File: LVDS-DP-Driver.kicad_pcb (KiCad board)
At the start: 2 copper layers, 50 x 50 mm, 122 parts, among them J1 47272-0001, J2 Conn_02x15_Odd_Even, J3 Conn_01x06_Male, J4 Conn_01x03_Male, J5 Conn_01x04_Male, J6 Conn_01x03_Male, Q1 Si4816BDY, Q10 2N7002, Q2 Si4816BDY, Q3 Si4816BDY, Q4 MMBT3904, Q5 MMBT3904, Q6 2N7002, Q7 AO3401A, Q8 2N7002, Q9 2N7002, SW1 SW_DIP_x04, U1 CS5211, U2 LTC3853, U3 AT24C64

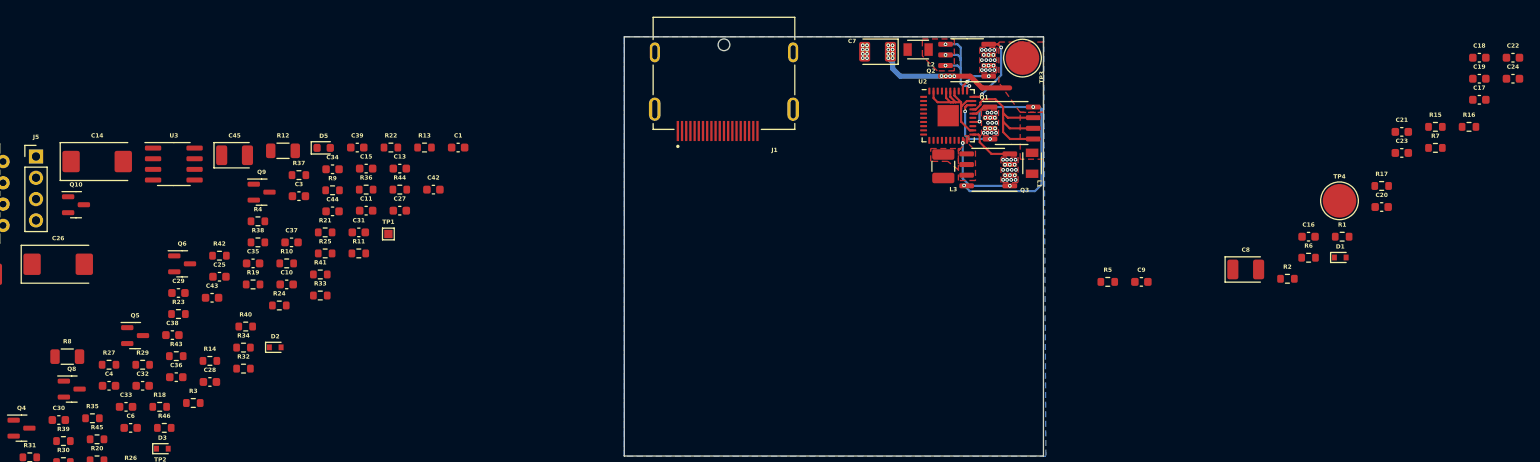
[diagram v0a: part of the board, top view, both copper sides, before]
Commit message: Buck layout 60%
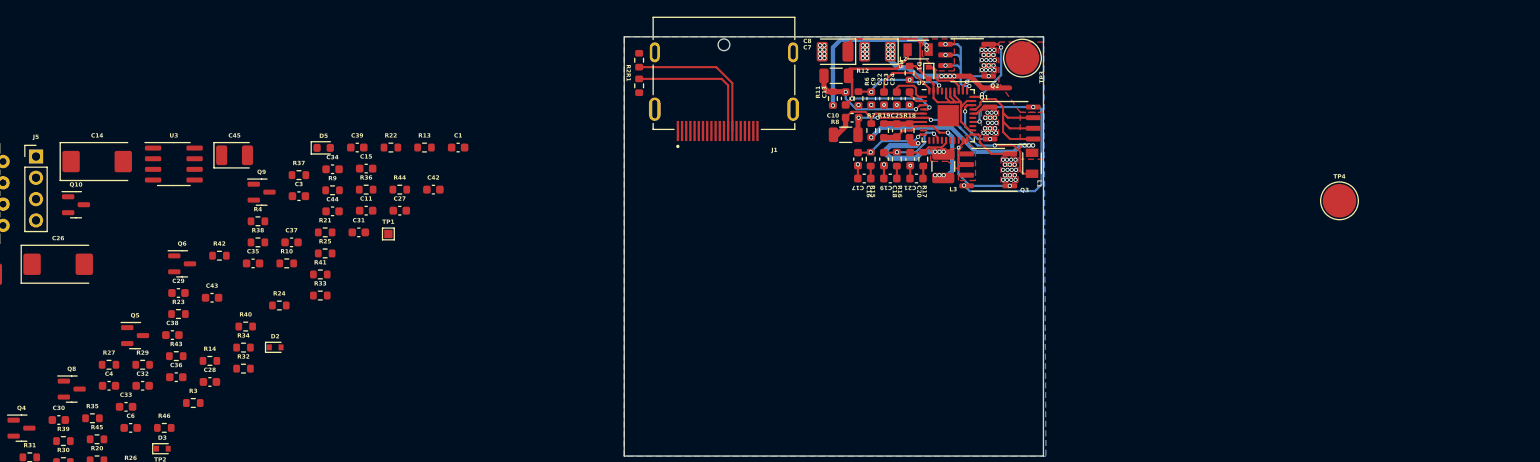
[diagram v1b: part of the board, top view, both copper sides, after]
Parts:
- moved R8 96.5 mm to (151.1, 27.4)
- moved R18 95.3 mm to (158.8, 26.9), turned to 90 degrees
- moved R1 85.8 mm to (126.5, 21.6), turned to -90 degrees
- moved C25 82.7 mm to (157.2, 26.9), turned to -90 degrees
- moved R2 81.6 mm to (126.5, 18.5), turned to 90 degrees
- moved R19 77.5 mm to (155.7, 26.9), turned to -90 degrees
- moved C22 75.2 mm to (155.7, 23.1), turned to -90 degrees
- moved C17 74.0 mm to (153.3, 32.6), turned to 180 degrees
- moved C18 72.0 mm to (155.7, 30.3), turned to -90 degrees
- moved C24 72.0 mm to (158.8, 23.1), turned to 90 degrees
- moved C19 71.3 mm to (156.4, 32.6), turned to 180 degrees
- moved C10 70.3 mm to (151.9, 25.4)
- moved R16 68.4 mm to (157.2, 30.3), turned to -90 degrees
- moved R15 67.5 mm to (154.1, 30.3), turned to -90 degrees
- moved R7 67.3 mm to (154.2, 26.9), turned to 90 degrees
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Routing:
- net +3V3: track 0.00 -> 27.0 mm, vias 0 -> 4
- net +5V: track 0.00 -> 23.8 mm, vias 0 -> 2
- net Net-(Q1-C): track 19.8 -> 41.1 mm, vias 0 -> 4
- net Net-(Q2-C): track 12.3 -> 31.6 mm, vias 4 -> 7
- net Net-(D1-A): track 15.6 -> 33.5 mm
- net Net-(J1-Pad14): track 0.00 -> 17.6 mm
- net Net-(J1-Pad13): track 0.00 -> 16.4 mm
- net +1V8: track 0.00 -> 15.5 mm, vias 0 -> 4
- net /SEN1+: track 0.00 -> 15.0 mm, vias 0 -> 2
- net /SEN2+: track 0.00 -> 13.7 mm
- net /SW3: track 0.00 -> 13.6 mm, vias 0 -> 4
- net Net-(U2-FREQ): track 0.00 -> 11.4 mm, vias 0 -> 3
- net Net-(U2-ITH1): track 0.00 -> 8.65 mm, vias 0 -> 2
- net Net-(U2-ITH2): track 0.00 -> 8.56 mm, vias 0 -> 2
- net Net-(U2-SS1): track 0.00 -> 8.15 mm
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
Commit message: Buck Components
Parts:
- moved C12 126.0 mm to (172.2, 39.4), turned to -90 degrees
- moved C26 99.4 mm to (156.5, 37.3), turned to 180 degrees
- moved D3 97.6 mm to (156.7, 20.8)
- moved C28 93.4 mm to (166.1, 35.3)
- moved D2 91.0 mm to (168.9, 22.6)
- moved R20 88.3 mm to (143.1, 31.8), turned to -90 degrees
- moved C29 86.2 mm to (153.9, 20.8), turned to 180 degrees
- moved R14 77.9 mm to (150.1, 32.6)
- moved R10 63.4 mm to (147.1, 32.6)
- moved R9 58.0 mm to (147.8, 30.3), turned to -90 degrees
- moved R21 56.2 mm to (144.7, 31.8), turned to 90 degrees
- moved C15 55.4 mm to (149.4, 30.3), turned to -90 degrees
- moved C11 52.7 mm to (146.3, 30.3), turned to -90 degrees
- moved R13 50.0 mm to (150.9, 30.3), turned to -90 degrees
- moved C14 49.7 mm to (111.5, 28.2), turned to 90 degrees
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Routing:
- net Net-(D3-K): track 0.00 -> 42.0 mm, vias 0 -> 2
- net Net-(D2-K): track 0.00 -> 40.3 mm, vias 0 -> 3
- net Net-(D1-K): track 5.59 -> 34.5 mm, vias 0 -> 4
- net /FB2: track 0.00 -> 28.0 mm, vias 0 -> 2
- net GND: track 4.63 -> 32.1 mm, vias 76 -> 169
- net /FB3: track 0.00 -> 27.3 mm, vias 0 -> 2
- net Net-(D1-A): track 33.5 -> 59.2 mm, vias 0 -> 5
- net +1V8: track 15.5 -> 39.3 mm, vias 4 -> 7
- net /FB1: track 0.00 -> 15.4 mm, vias 0 -> 2
- net /SW3: track 13.6 -> 28.9 mm
- net +3V3: track 27.0 -> 39.8 mm, vias 4 -> 5
- net +5V: track 23.8 -> 33.3 mm, vias 2 -> 4
- net Net-(Q2-C): track 31.6 -> 39.4 mm, vias 7 -> 8
- net Net-(Q1-C): track 41.1 -> 48.0 mm
- net +12V: track 49.8 -> 48.5 mm, vias 15 -> 13
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- added copper zone on F.Cu, net +1V8
- added copper zone on F.Cu, net +3V3
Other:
- board text added: "-L-"
- board text added: "-M-"
- board text added: "-R-"

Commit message: LVDS routing and layouting misc
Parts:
- added G0: R_0603_1608Metric, Resistor_SMD:R_0603_1608Metric, F.Cu at (159.0, 44.7)
- added G1: R_0603_1608Metric, Resistor_SMD:R_0603_1608Metric, F.Cu at (161.5, 44.7)
- added G2: R_0603_1608Metric, Resistor_SMD:R_0603_1608Metric, F.Cu at (164.1, 44.7)
- added G3: R_0603_1608Metric, Resistor_SMD:R_0603_1608Metric, F.Cu at (166.6, 44.7)
- J3: footprint Connector_PinHeader_2.54mm:PinHeader_1x06_P2.54mm_Vertical -> Connector_PinHeader_2.00mm:PinHeader_1x06_P2.00mm_Vertical
- moved J3 132.4 mm to (167.8, 60.7), turned to -90 degrees
- moved J2 124.1 mm to (154.2, 55.1), turned to -90 degrees
- moved J5 120.8 mm to (172.7, 55.1), turned to 180 degrees
- moved J6 117.9 mm to (161.6, 53.8), turned to 90 degrees
- moved SW1 117.4 mm to (159.0, 48.5), turned to 90 degrees
- moved J4 115.6 mm to (154.7, 46.5)
- moved R28 111.1 mm to (167.4, 50.5), turned to 180 degrees
- moved R31 105.6 mm to (158.2, 50.5)
- moved R30 104.7 mm to (161.3, 50.5)
- moved U1 102.4 mm to (135.2, 40.4)
- moved Q10 100.7 mm to (157.7, 56.9)
- moved R29 97.2 mm to (164.3, 50.5)
- moved C5 92.5 mm to (138.9, 32.3), turned to -90 degrees
- moved D4 91.0 mm to (125.6, 28.7), turned to 90 degrees
- moved C45 88.5 mm to (162.3, 57.4), turned to 180 degrees
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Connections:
- net Net-(U1A-AUXN) renamed AUXN
- net Net-(U1A-AUXP) renamed AUXP
- net Net-(U1A-DP0N) renamed DP0N
- net Net-(U1A-DP0P) renamed DP0P
- net Net-(U1A-DP1N) renamed DP1N
- net Net-(U1A-DP1P) renamed DP1P
- J4 pad 3: +3.3V -> +3V3
- Q6 pad 1: +3.3V -> +3V3
- R22 pad 1: +3.3V -> +3V3
- R27 pad 1: +3.3V -> +3V3
- R28 pad 1: +3.3V -> +3V3
- R29 pad 1: +3.3V -> +3V3
- R30 pad 1: +3.3V -> +3V3
- R31 pad 1: +3.3V -> +3V3
- R39 pad 1: +3.3V -> +3V3
- R40 pad 1: +3.3V -> +3V3
- R41 pad 1: +3.3V -> +3V3
- R42 pad 1: +3.3V -> +3V3
- R43 pad 1: +3.3V -> +3V3
- R44 pad 1: +3.3V -> +3V3
- R45 pad 2: +3.3V -> +3V3
- R46 pad 2: +3.3V -> +3V3
- U3 pad 8: +3.3V -> +3V3
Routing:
- net +5V: track 33.3 -> 165.8 mm, vias 4 -> 16
- net +3V3: track 39.8 -> 153.3 mm, vias 5 -> 14
- net /BLDN: track 0.00 -> 90.3 mm, vias 0 -> 7
- net +1V8: track 39.3 -> 117.6 mm, vias 7 -> 10
- net /PWRDN: track 0.00 -> 61.7 mm, vias 0 -> 3
- net /BKUP_BTN: track 0.00 -> 57.6 mm, vias 0 -> 3
- net GND: track 32.1 -> 82.8 mm, vias 169 -> 240
- net /EN_BKLT: track 0.00 -> 40.6 mm, vias 0 -> 2
- net +12V: track 48.5 -> 83.9 mm, vias 13 -> 14
- net /GPIO3: track 0.00 -> 34.8 mm, vias 0 -> 2
- net /GPIO2: track 0.00 -> 32.5 mm, vias 0 -> 2
- net /GPIO1: track 0.00 -> 29.9 mm, vias 0 -> 2
- net /GPIO0: track 0.00 -> 28.1 mm, vias 0 -> 2
- net /P_BKLT_EN: track 0.00 -> 25.4 mm
- net /E2_SDA: track 0.00 -> 23.3 mm, vias 0 -> 2
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- added copper zone on F.Cu, net /LCD_BKLT_VCC
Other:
- board size 50 x 50 mm -> 50 x 46.7 mm
- board text added: "U"

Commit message: Finished routing
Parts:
- moved Q7 97.5 mm to (145.3, 50.3), turned to 180 degrees
- moved Q8 85.3 mm to (144.1, 60.5)
- moved C38 82.4 mm to (146.6, 18.8), turned to 90 degrees
- moved R35 80.1 mm to (141.4, 60.3), turned to 90 degrees
- moved C30 77.4 mm to (134.6, 60.2), turned to 90 degrees
- moved C39 73.6 mm to (165.9, 38.4)
- moved C40 73.4 mm to (137.9, 60.5), turned to 180 degrees
- moved Q9 71.6 mm to (148.1, 60.5), turned to 180 degrees
- moved C33 64.8 mm to (130.0, 60.2), turned to 90 degrees
- moved C32 64.4 mm to (131.6, 60.2), turned to 90 degrees
- moved R34 63.3 mm to (142.5, 50.0), turned to 90 degrees
- moved C37 63.2 mm to (147.1, 27.9)
- moved R33 59.7 mm to (148.1, 50.3), turned to -90 degrees
- moved C36 54.3 mm to (125.5, 60.2), turned to -90 degrees
- moved R36 50.5 mm to (142.7, 47.0), turned to 90 degrees
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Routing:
- net +3V3: track 153.3 -> 233.5 mm, vias 14 -> 20
- net +1V8: track 117.6 -> 177.1 mm, vias 10 -> 17
- net /EN_VCC: track 0.00 -> 56.3 mm, vias 0 -> 6
- net HT: track 7.96 -> 53.4 mm, vias 0 -> 13
- net /PWM0: track 4.55 -> 46.5 mm, vias 2 -> 6
- net Net-(Q8-D): track 0.00 -> 34.3 mm, vias 0 -> 2
- net Net-(Q9-D): track 0.00 -> 30.5 mm, vias 0 -> 2
- net GND: track 82.8 -> 99.2 mm, vias 240 -> 280
- net Net-(J4-Pin_2): track 0.00 -> 9.52 mm, vias 0 -> 1
- net /B0N: track 12.3 -> 21.4 mm
- net /A3N: track 12.6 -> 21.4 mm
- net /ACLKN: track 13.1 -> 21.2 mm
- net /B1N: track 13.8 -> 21.3 mm
- net /B0P: track 14.9 -> 21.5 mm
- net /B2N: track 14.9 -> 21.2 mm
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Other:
- outline, holes or cut-outs redrawn

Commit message: Changed License to SHL
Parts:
- added REF**: OSHW-Logo_5.7x6mm_SilkScreen, Symbol:OSHW-Logo_5.7x6mm_SilkScreen, F.Cu at (131.1, 48.5)
- added REF**: Symbol_Highvoltage_Type1_CopperTop_Small, Symbol:Symbol_Highvoltage_Type1_CopperTop_Small, B.Cu at (130.6, 19.6)
- added REF**: OSHW-Logo2_7.3x6mm_Copper, Symbol:OSHW-Logo2_7.3x6mm_Copper, B.Cu at (139.2, 19.1)

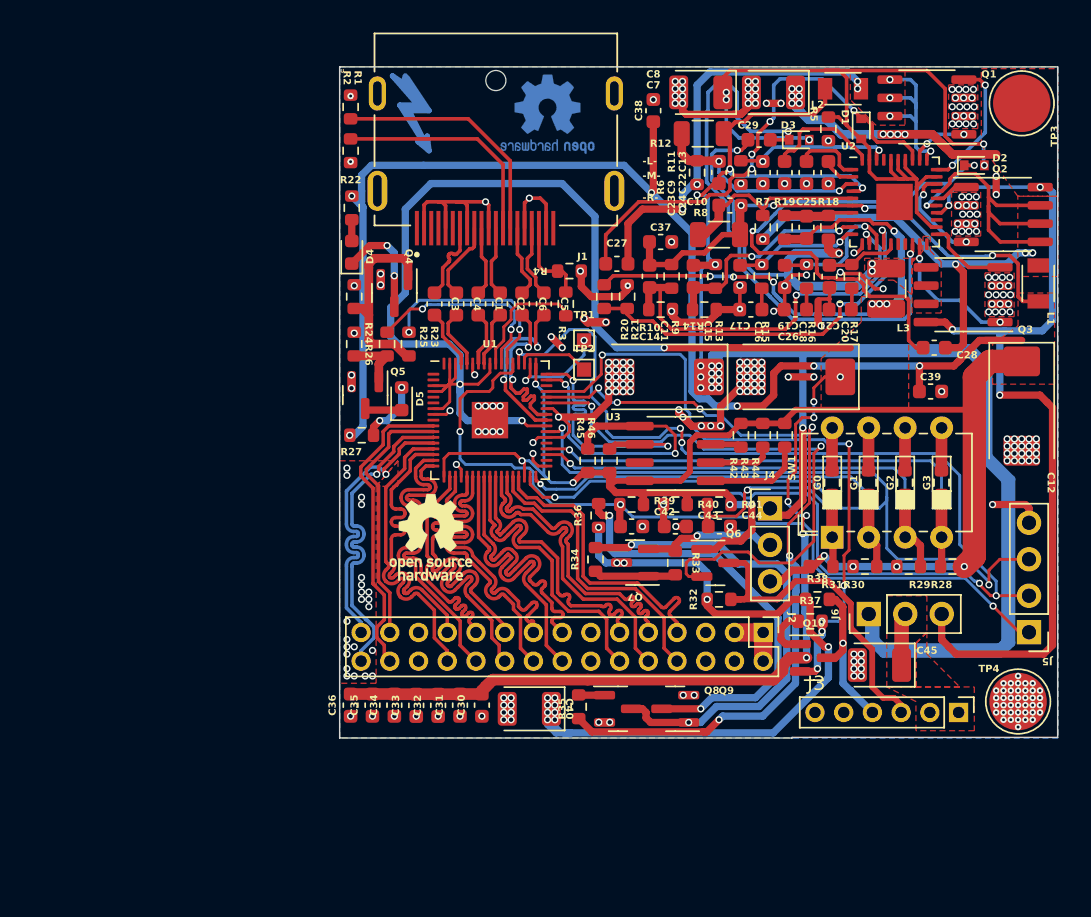
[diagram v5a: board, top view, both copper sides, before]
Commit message: assigned footprints
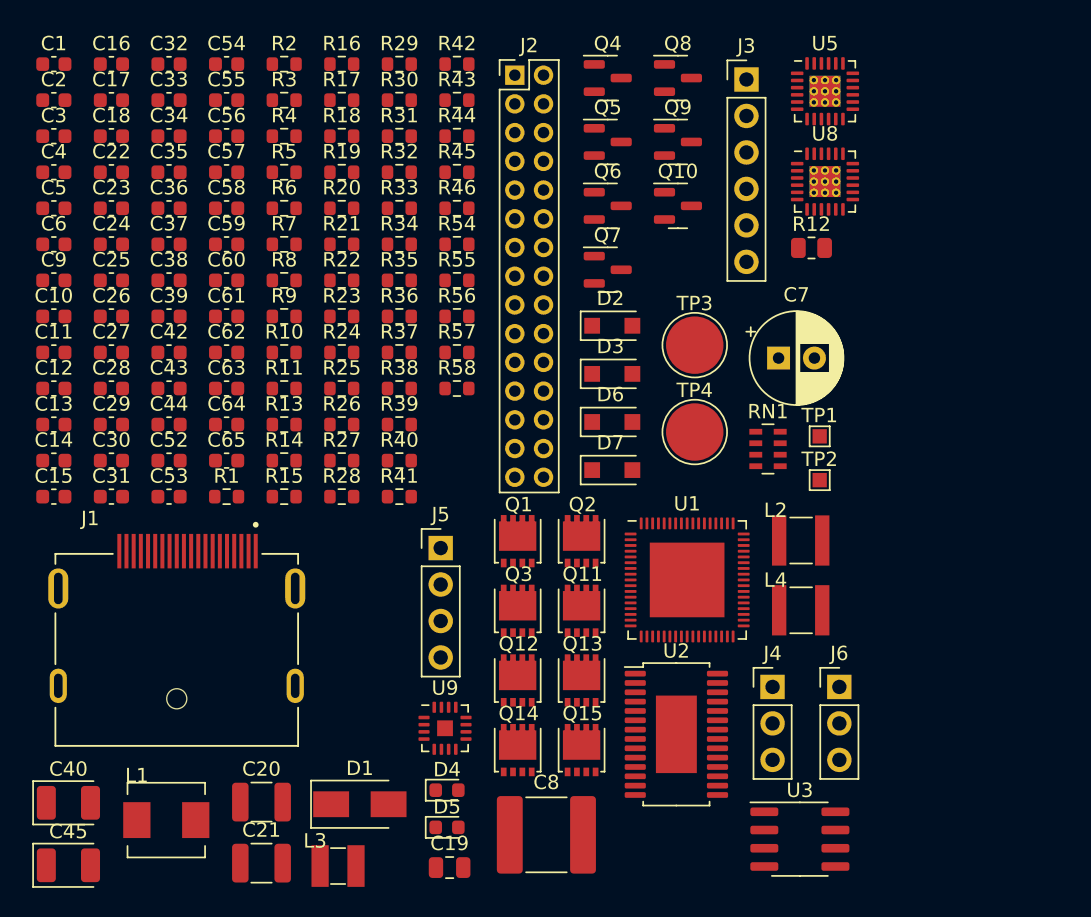
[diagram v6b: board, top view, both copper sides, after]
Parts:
- removed G0, G1, G2, G3: R_0603_1608Metric, Resistor_SMD:R_0603_1608Metric
- removed REF**: OSHW-Logo_5.7x6mm_SilkScreen, Symbol:OSHW-Logo_5.7x6mm_SilkScreen
- removed REF**: Symbol_Highvoltage_Type1_CopperTop_Small, Symbol:Symbol_Highvoltage_Type1_CopperTop_Small
- removed REF**: OSHW-Logo2_7.3x6mm_Copper, Symbol:OSHW-Logo2_7.3x6mm_Copper
- removed SW1: SW_DIP_x04, Button_Switch_THT:SW_DIP_SPSTx04_Slide_6.7x11.72mm_W7.62mm_P2.54mm_LowProfile
- added C52: 4.7nF, Capacitor_SMD:C_0603_1608Metric, F.Cu at (112.8, 43.2)
- added C53: 10uF, Capacitor_SMD:C_0603_1608Metric, F.Cu at (112.8, 45.7)
- added C54: 10uF, Capacitor_SMD:C_0603_1608Metric, F.Cu at (116.8, 15.6)
- added C55: 3.3nF, Capacitor_SMD:C_0603_1608Metric, F.Cu at (116.8, 18.1)
- added C56: 100nF, Capacitor_SMD:C_0603_1608Metric, F.Cu at (116.8, 20.6)
- added C57: 33pF, Capacitor_SMD:C_0603_1608Metric, F.Cu at (116.8, 23.1)
- added C58: 2.2uF, Capacitor_SMD:C_0603_1608Metric, F.Cu at (116.8, 25.6)
- added C59: 39nF, Capacitor_SMD:C_0603_1608Metric, F.Cu at (116.8, 28.1)
- added C60: 220nF, Capacitor_SMD:C_0603_1608Metric, F.Cu at (116.8, 30.6)
- added C61: 100nF, Capacitor_SMD:C_0603_1608Metric, F.Cu at (116.8, 33.1)
- added C62: 220pF, Capacitor_SMD:C_0603_1608Metric, F.Cu at (116.8, 35.6)
- added C63: 10uF, Capacitor_SMD:C_0603_1608Metric, F.Cu at (116.8, 38.1)
- added C64: 100nF, Capacitor_SMD:C_0603_1608Metric, F.Cu at (116.8, 40.7)
- added C65: 22uF, Capacitor_SMD:C_0603_1608Metric, F.Cu at (116.8, 43.2)
- added D6: DSK12, Diode_SMD:D_SOD-123F, F.Cu at (143.7, 40.5)
- added D7: DSK12, Diode_SMD:D_SOD-123F, F.Cu at (143.7, 43.8)
- added L4: CKST353220-2.2uH/M, Footprints:CKST353220, F.Cu at (155.1, 52.0)
- added Q11: AGM612AP, Footprints:PDFN8_3x3, F.Cu at (141.6, 53.6)
- added Q12: AGM308AP, Footprints:PDFN8_3x3, F.Cu at (137.2, 58.5)
- added Q13: AGM308AP, Footprints:PDFN8_3x3, F.Cu at (141.6, 58.5)
- added Q14: AGM308AP, Footprints:PDFN8_3x3, F.Cu at (137.2, 63.3)
- added Q15: AGM308AP, Footprints:PDFN8_3x3, F.Cu at (141.6, 63.3)
- added R54: 10R, Resistor_SMD:R_0603_1608Metric, F.Cu at (132.9, 28.1)
- added R55: 2K32, Resistor_SMD:R_0603_1608Metric, F.Cu at (132.9, 30.6)
- added R56: 10K, Resistor_SMD:R_0603_1608Metric, F.Cu at (132.9, 33.1)
- added R57: 187K, Resistor_SMD:R_0603_1608Metric, F.Cu at (132.9, 35.6)
- added R58: 150K, Resistor_SMD:R_0603_1608Metric, F.Cu at (132.9, 38.1)
- added RN1: R_Pack04, Resistor_SMD:R_Array_Concave_4x0603, F.Cu at (154.5, 42.4)
- added U5: LM25141, Package_DFN_QFN:QFN-24-1EP_4x4mm_P0.5mm_EP2.15x2.15mm_ThermalVias, F.Cu at (158.5, 17.4)
- added U8: LM25141, Package_DFN_QFN:QFN-24-1EP_4x4mm_P0.5mm_EP2.15x2.15mm_ThermalVias, F.Cu at (158.5, 23.7)
- added U9: TLV62130, Package_DFN_QFN:VQFN-16-1EP_3x3mm_P0.5mm_EP1.1x1.1mm, F.Cu at (132.1, 61.8)
- C10: value 100nF -> 15nF
- C11: value 10pF -> 100pF
- C12: value 330uF -> 6.8nF; footprint Capacitor_Tantalum_SMD:CP_EIA-7343-31_Kemet-D -> Capacitor_SMD:C_0603_1608Metric
- C13: value 100nF -> 82pF
- C14: value 330uF -> 100nF; footprint Capacitor_Tantalum_SMD:CP_EIA-7343-31_Kemet-D -> Capacitor_SMD:C_0603_1608Metric
- C15: value 10pF -> 47pF
- C16: value 220pF -> 100nF
- C17: value 1.5nF -> 100nF
- C18: value 220pF -> 1uF
- C19: value 1.5nF -> 22uF * 3; footprint Capacitor_SMD:C_0603_1608Metric -> Capacitor_SMD:C_0805_2012Metric
- C20: value 330pF -> 47uF; footprint Capacitor_SMD:C_0603_1608Metric -> Capacitor_SMD:C_1210_3225Metric
- C21: value 1.5nF -> 47uF; footprint Capacitor_SMD:C_0603_1608Metric -> Capacitor_SMD:C_1210_3225Metric
- C22: value 100nF -> 10uF
- C24: value 100nF -> 39nF
- C25: value 68nF -> 220nF
- C26: value 330uF -> 2.2uF; footprint Capacitor_Tantalum_SMD:CP_EIA-7343-31_Kemet-D -> Capacitor_SMD:C_0603_1608Metric
- C28: value 100nF -> 4.7uF
- C29: value 100nF -> 56pF
- C7: value 22uF -> 68uF; footprint Capacitor_Tantalum_SMD:CP_EIA-3528-21_Kemet-B -> Capacitor_THT:CP_Radial_D6.3mm_P2.50mm
- C8: value 4.7uF -> 10uF * 3; footprint Capacitor_Tantalum_SMD:CP_EIA-3528-21_Kemet-B -> Capacitor_SMD:C_2220_5650Metric
- C9: value 1nF -> 100nF
- D1: value D_Schottky -> MBR180S1-7; footprint Diode_SMD:D_SOD-523 -> Diode_SMD:D_SMA
- D2: value D_Schottky -> DSK12; footprint Diode_SMD:D_SOD-523 -> Diode_SMD:D_SOD-123F
- D3: value D_Schottky -> RB160MM-90TR; footprint Diode_SMD:D_SOD-523 -> Diode_SMD:D_SOD-123F
- J3: footprint Connector_PinHeader_2.00mm:PinHeader_1x06_P2.00mm_Vertical -> Connector_PinHeader_2.54mm:PinHeader_1x06_P2.54mm_Vertical
- L1: value 3.3uH -> CYA0650-3.3UH; footprint Inductor_SMD:L_TDK_NLV25_2.5x2.0mm -> Footprints:L_0530
- L2: value 3.3uH -> CKST353220-2.2uH/M; footprint Inductor_SMD:L_TDK_NLV25_2.5x2.0mm -> Footprints:CKST353220
- L3: value 1.5uH -> CKST322512-1uH/M; footprint Inductor_SMD:L_1210_3225Metric -> Footprints:CKST322512
- Q1, Q2, Q3: value Si4816BDY -> AGM612AP; footprint Package_SO:SO-8_3.9x4.9mm_P1.27mm -> Footprints:PDFN8_3x3
- R10: value 20K -> 93K1
- R11: value 4.75K -> 13K
- R12: value 1430 -> 15m; footprint Resistor_SMD:R_1206_3216Metric -> Resistor_SMD:R_0805_2012Metric
- R13: value 105K -> 100R
- R14: value 20K -> 100R
- R15: value 15K -> 10K
- R16: value 18K -> 280K
- R17: value 10K -> 20K
- R18: value 2.43K -> 10R
- R19: value 1.82K -> 12m
- R20: value 25K -> 1K62
- R21: value 20K -> 10m
- R5: value 10K -> 249K
- R6: value 3.16K -> 42K2
- R7: value 4.75K -> 2K
- R8: value 1430 -> 10R; footprint Resistor_SMD:R_1206_3216Metric -> Resistor_SMD:R_0603_1608Metric
- R9: value 63.4K -> 6K19
- U2: value LTC3853 -> LM5176; footprint Package_DFN_QFN:QFN-40-1EP_6x6mm_P0.5mm_EP4.6x4.6mm -> Package_SO:HTSSOP-28-1EP_4.4x9.7mm_P0.65mm_EP2.85x5.4mm
- moved L1 71.8 mm to (110.6, 65.6), turned to 0 degrees
- moved C12 67.4 mm to (104.8, 38.1), turned to 0 degrees
- moved D1 58.6 mm to (126.1, 67.1), turned to 0 degrees
- moved C45 58.2 mm to (105.8, 71.3), turned to 0 degrees
- moved C28 57.4 mm to (108.8, 38.1)
- moved C21 55.8 mm to (119.3, 71.2), turned to 0 degrees
- moved L3 55.7 mm to (123.0, 70.2), turned to 0 degrees
- moved J1 54.4 mm to (113.4, 63.0), turned to 0 degrees
- moved C20 53.9 mm to (119.3, 66.9), turned to 0 degrees
- moved C39 53.3 mm to (112.8, 33.1)
- moved C8 52.8 mm to (139.1, 69.2), turned to 0 degrees
- moved C24 50.2 mm to (108.8, 28.1), turned to 0 degrees
- moved C9 49.9 mm to (104.8, 30.6), turned to 0 degrees
- moved R29 49.8 mm to (128.9, 15.6)
- moved C13 49.5 mm to (104.8, 40.7), turned to 0 degrees
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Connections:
- net /TG3 renamed /HDRV2
- net AUXN renamed Net-(U1A-AUXN)
- net AUXP renamed Net-(U1A-AUXP)
- net DP0N renamed Net-(U1A-DP0N)
- net DP0P renamed Net-(U1A-DP0P)
- net DP1N renamed Net-(U1A-DP1N)
- net DP1P renamed Net-(U1A-DP1P)
- C10 pad 1: /SEN2+ -> GND
- C10 pad 2: +3V3 -> Net-(U2-SS)
- C11 pad 1: +3V3 -> GND
- C11 pad 2: /FB2 -> Net-(U2-COMP)
- C12 pad 1: +3V3 -> Net-(C12-Pad1)
- C12 pad 2: GND -> Net-(U2-COMP)
- C13 pad 1: /SEN1+ -> Net-(U2-SLOPE)
- C13 pad 2: +5V -> GND
- C14 pad 1: +5V -> Net-(U2-BIAS)
- C15 pad 1: +5V -> Net-(U2-CSG)
- C15 pad 2: /FB1 -> Net-(U2-CS)
- C16 pad 1: Net-(U2-ITH1) -> /SW2
- C16 pad 2: GND -> Net-(D2-K)
- C17 pad 1: Net-(C17-Pad1) -> Net-(D3-K)
- C17 pad 2: GND -> /SW1
- C18 pad 1: Net-(U2-ITH2) -> /VCC
- C19 pad 1: Net-(C19-Pad1) -> +12V
- C20 pad 1: Net-(U2-ITH3) -> +12V
- C21 pad 1: Net-(C21-Pad1) -> +12V
- C22 pad 1: Net-(U2-SS1) -> +12V
- C23 pad 1: GND -> Net-(U5-DEMB)
- C23 pad 2: Net-(U2-SS2) -> GND
- C24 pad 1: GND -> Net-(U5-SS)
- C24 pad 2: Net-(U2-SS3) -> GND
- C25 pad 1: /SEN3+ -> Net-(U5-RES)
- C25 pad 2: +1V8 -> GND
- C26 pad 1: +1V8 -> /BUCK5_BIASVCC
- C27 pad 1: Net-(D1-K) -> /BUCK5_SW
- C27 pad 2: Net-(Q2-C) -> Net-(D6-K)
- C28 pad 1: Net-(D2-K) -> +5V
- C28 pad 2: Net-(Q1-C) -> GND
- C29 pad 1: Net-(D3-K) -> Net-(U5-COMP)
- C29 pad 2: /SW3 -> GND
- C37 pad 1: +3V3 -> +3.3V
- C38 pad 1: +3V3 -> +3.3V
- C39 pad 1: +3V3 -> +3.3V
- C7 pad 1: +12V -> VDC
- C8 pad 1: Net-(D1-A) -> VDC
- C9 pad 1: Net-(U2-FREQ) -> Net-(U2-VIN)
- D1 pad 2: Net-(D1-A) -> VDC
- D2 pad 2: Net-(D1-A) -> /VCC
- D3 pad 2: Net-(D1-A) -> /VCC
- J4 pad 3: +3V3 -> +3.3V
- L1 pad 1: Net-(Q1-C) -> /SW1
- L1 pad 2: +3V3 -> /SW2
- L2 pad 1: Net-(Q2-C) -> /BUCK5_SW
- L2 pad 2: +5V -> /CS_5
- L3 pad 1: /SW3 -> /BUCK3_SW
- L3 pad 2: +1V8 -> /CS_3
- Q1 pad 1: Net-(Q1-G1) -> /HDRV1
- Q1 pad 2: GND -> /SW1
- Q1 pad 3: GND -> VDC
- Q2 pad 1: Net-(Q2-G1) -> /LDRV1
- Q2 pad 2: GND -> /RCS
- Q2 pad 3: GND -> /SW1
- Q3 pad 2: GND -> /SW2
- Q3 pad 3: GND -> +12V
- Q6 pad 1: +3V3 -> +3.3V
- R10 pad 1: /FB2 -> GND
- R10 pad 2: GND -> Net-(U2-MODE)
- R11 pad 1: Net-(Q2-C) -> GND
- R11 pad 2: /SEN1+ -> Net-(U2-SYNC)
- R12 pad 1: /SEN1+ -> GND
- R12 pad 2: +5V -> /RCS
- R13 pad 1: +5V -> GND
- R13 pad 2: /FB1 -> Net-(U2-CSG)
- R14 pad 1: /FB1 -> /RCS
- R14 pad 2: GND -> Net-(U2-CS)
- R15 pad 1: Net-(U2-ITH1) -> /VCC
- R15 pad 2: Net-(C17-Pad1) -> /MAIN_PG
- R16 pad 1: Net-(U2-ITH2) -> +12V
- R16 pad 2: Net-(C19-Pad1) -> /MAINPWR_FB
- R17 pad 1: Net-(U2-ITH3) -> /MAINPWR_FB
- R17 pad 2: Net-(C21-Pad1) -> GND
- R18 pad 1: /SW3 -> Net-(U5-HO)
- R18 pad 2: /SEN3+ -> /HDRV_5
- R19 pad 1: /SEN3+ -> /CS_5
- R19 pad 2: +1V8 -> +5V
- R20 pad 1: +1V8 -> Net-(C52-Pad2)
- R20 pad 2: /FB3 -> GND
- R21 pad 1: /FB3 -> /CS_3
- R21 pad 2: GND -> +3V3
- R22 pad 1: +3V3 -> +3.3V
- R27 pad 1: +3V3 -> +3.3V
- R28 pad 1: +3V3 -> +3.3V
- R29 pad 1: +3V3 -> +3.3V
- R30 pad 1: +3V3 -> +3.3V
- R31 pad 1: +3V3 -> +3.3V
- R39 pad 1: +3V3 -> +3.3V
- R40 pad 1: +3V3 -> +3.3V
- R41 pad 1: +3V3 -> +3.3V
- R42 pad 1: +3V3 -> +3.3V
- R43 pad 1: +3V3 -> +3.3V
- R44 pad 1: +3V3 -> +3.3V
- R45 pad 2: +3V3 -> +3.3V
- R46 pad 2: +3V3 -> +3.3V
- R5 pad 1: Net-(D1-A) -> VDC
- R5 pad 2: Net-(U2-FREQ) -> /ENABLE
- R6 pad 1: Net-(U2-FREQ) -> /ENABLE
- R7 pad 1: Net-(Q1-C) -> VDC
- R7 pad 2: /SEN2+ -> /VINSNS
- R8 pad 1: /SEN2+ -> Net-(D1-K)
- R8 pad 2: +3V3 -> Net-(U2-VIN)
- R9 pad 1: +3V3 -> GND
- R9 pad 2: /FB2 -> Net-(C12-Pad1)
- U1 pad 18: +3V3 -> +3.3V
- U1 pad 32: +3V3 -> +3.3V
- U1 pad 52: +3V3 -> +3.3V
- U1 pad 63: GND -> (no net)
- U2 pad 1: Net-(U2-SS2) -> /ENABLE
- U2 pad 10: Net-(U2-ITH1) -> GND
- U2 pad 11: GND -> /MAINPWR_FB
- U2 pad 12: /FB2 -> +12V
- U2 pad 13: Net-(U2-ITH2) -> GND
- U2 pad 14: /FB3 -> GND
- U2 pad 15: Net-(U2-ITH3) -> Net-(U2-CSG)
- U2 pad 16: unconnected-(U2-PG3) -> Net-(U2-CS)
- U2 pad 17: unconnected-(U2-PG12) -> /MAIN_PG
- U2 pad 18: Net-(D3-K) -> /SW2
- U2 pad 2: Net-(U2-SS3) -> Net-(U2-VIN)
- U2 pad 20: /SW3 -> Net-(D2-K)
- U2 pad 21: /BG3 -> /LDRV2
- U2 pad 22: Net-(D1-A) -> GND
- U2 pad 23: unconnected-(U2-EXTVcc) -> /VCC
- U2 pad 24: +12V -> Net-(U2-BIAS)
- U2 pad 25: Net-(D2-K) -> /LDRV1
- U2 pad 26: Net-(Q1-G1) -> Net-(D3-K)
- U2 pad 27: Net-(Q1-C) -> /HDRV1
- U2 pad 28: Net-(Q1-G2) -> /SW1
- U2 pad 29: Net-(D1-A) -> (no net)
- U2 pad 3: /SEN1+ -> /VINSNS
- U2 pad 4: +5V -> Net-(U2-MODE)
- U2 pad 5: /SEN2+ -> GND
- U2 pad 6: +3V3 -> Net-(U2-SYNC)
- U2 pad 7: /SEN3+ -> Net-(U2-SLOPE)
- U2 pad 8: +1V8 -> Net-(U2-SS)
- U2 pad 9: /FB1 -> Net-(U2-COMP)
- U3 pad 8: +3V3 -> +3.3V
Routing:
- net +3V3: track 233.5 -> 0.00 mm, vias 20 -> 0
- net +1V8: track 177.1 -> 0.00 mm, vias 17 -> 0
- net +5V: track 170.1 -> 0.00 mm, vias 16 -> 0
- net GND: track 99.2 -> 0.00 mm, vias 280 -> 0
- net /BLDN: track 84.1 -> 0.00 mm, vias 6 -> 0
- net +12V: track 83.9 -> 0.00 mm, vias 14 -> 0
- net /PWRDN: track 61.1 -> 0.00 mm, vias 3 -> 0
- net Net-(D1-A): track 59.2 -> 0.00 mm, vias 5 -> 0
- net /BKUP_BTN: track 57.5 -> 0.00 mm, vias 3 -> 0
- net /EN_VCC: track 56.3 -> 0.00 mm, vias 6 -> 0
- net HT: track 53.4 -> 0.00 mm, vias 13 -> 0
- net Net-(Q1-C): track 48.0 -> 0.00 mm, vias 4 -> 0
- net /PWM0: track 46.5 -> 0.00 mm, vias 6 -> 0
- net Net-(D3-K): track 42.0 -> 0.00 mm, vias 2 -> 0
- net Net-(Q2-C): track 41.1 -> 0.00 mm, vias 8 -> 0
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- removed copper zone on F.Cu, net +12V
- removed copper zone on F.Cu, net +1V8
- removed copper zone on F.Cu, net +3V3
- removed copper zone on F.Cu, net /LCD_BKLT_VCC
- removed copper zone on F.Cu, net /SW3
- removed copper zone on B.Cu, net GND
- removed copper zone on F.Cu, net GND
- removed copper zone on F.Cu, net Net-(Q1-C)
- removed copper zone on F.Cu, net Net-(Q2-C)
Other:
- board outline removed
- board text removed: "-L-"
- board text removed: "-M-"
- board text removed: "-R-"
- board text removed: "U"
